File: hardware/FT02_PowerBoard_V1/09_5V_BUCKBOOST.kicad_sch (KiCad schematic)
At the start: 0 parts

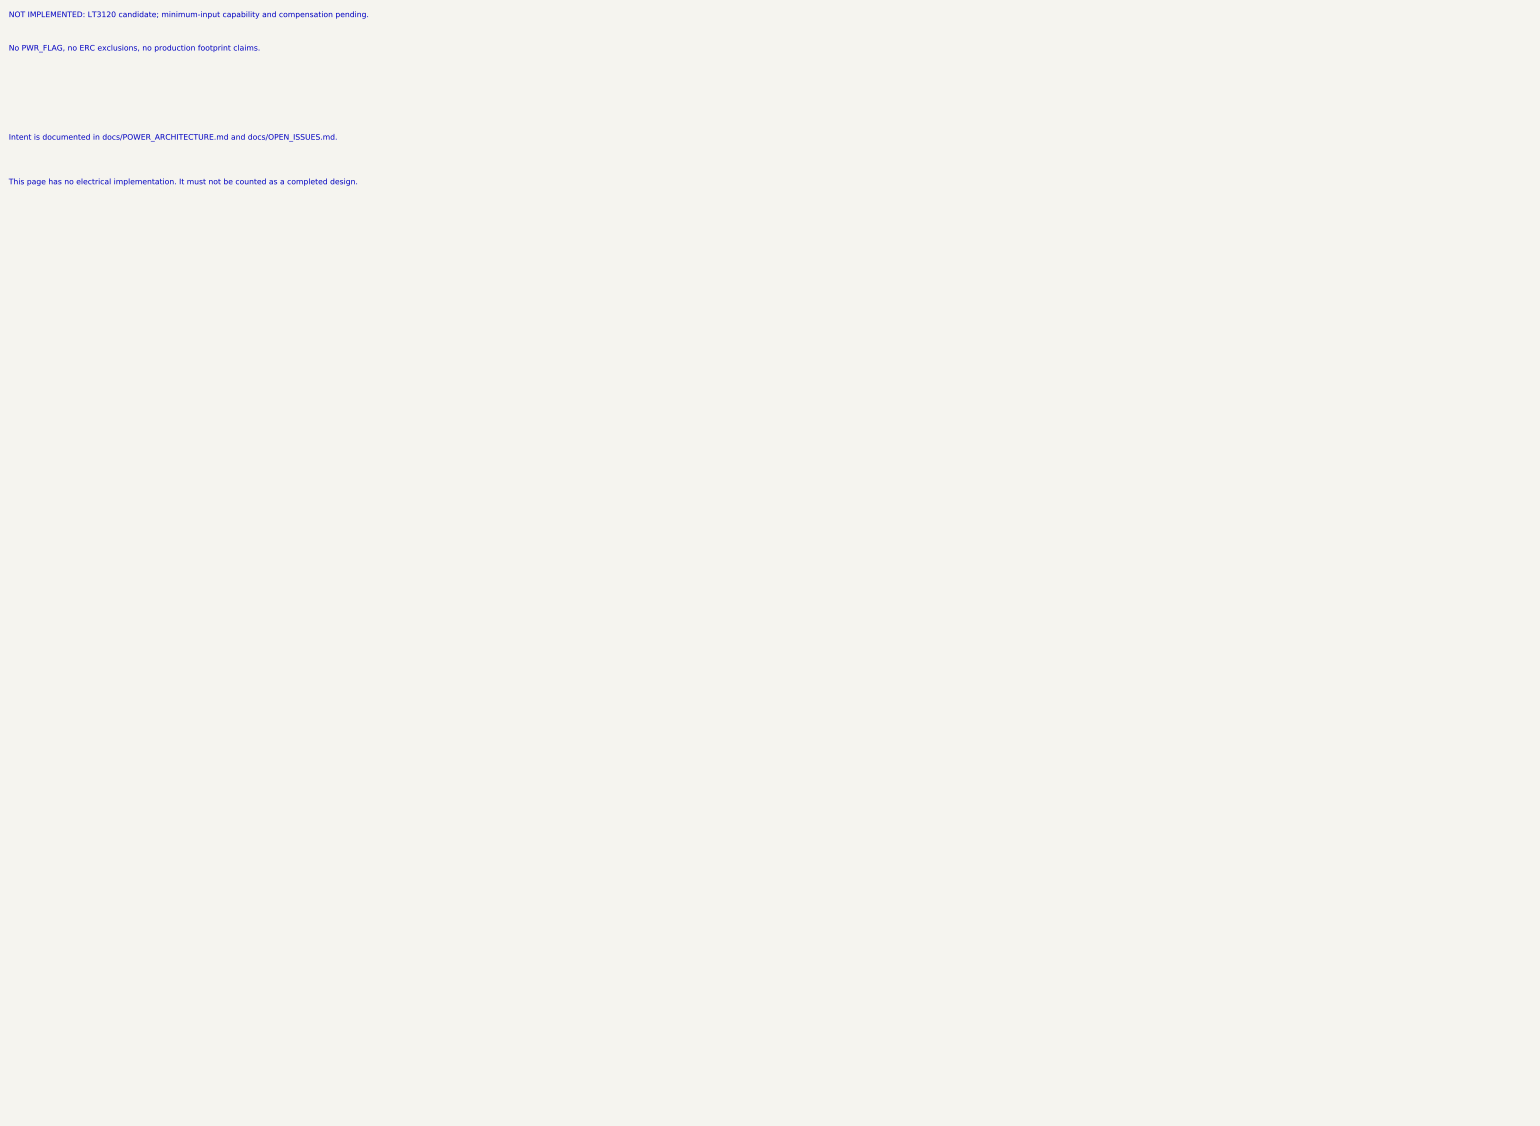
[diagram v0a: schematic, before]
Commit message: Wire FT02 Phase 1 power stages and verify partial shunt boundary
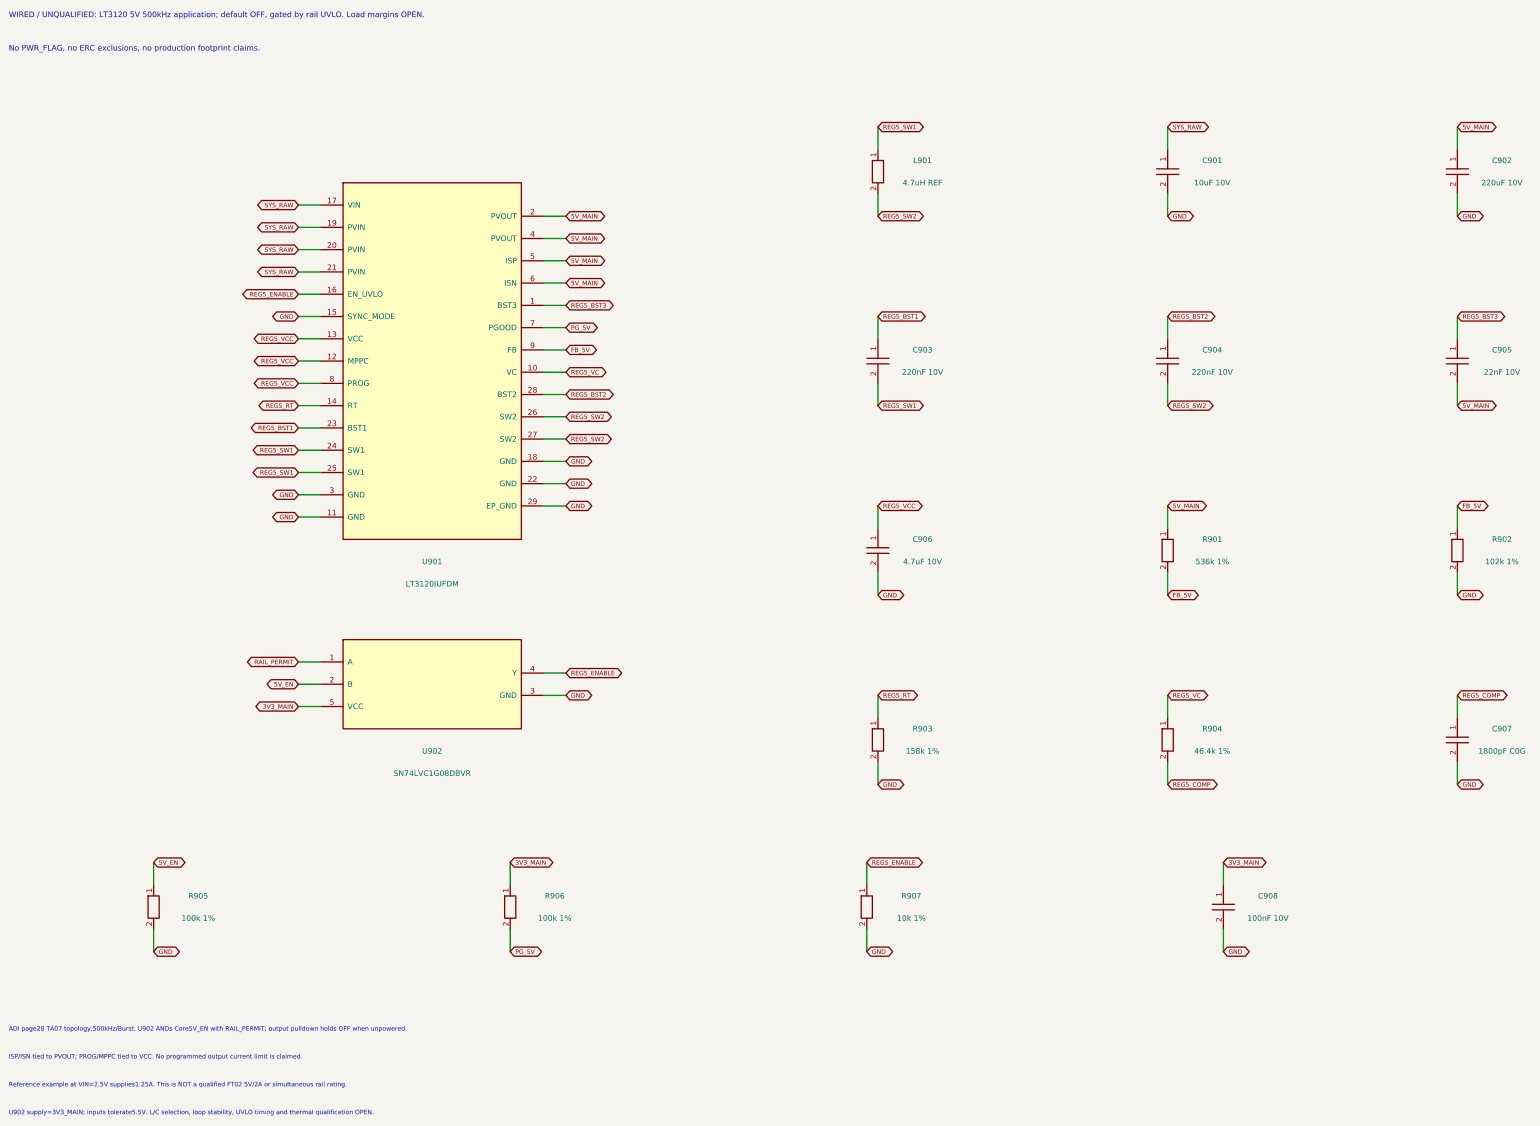
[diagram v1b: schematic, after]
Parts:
- added C901: 10uF 10V, symbol FT02_Reference:C
- added C902: 220uF 10V, symbol FT02_Reference:C
- added C903, C904: 220nF 10V, symbol FT02_Reference:C
- added C905: 22nF 10V, symbol FT02_Reference:C
- added C906: 4.7uF 10V, symbol FT02_Reference:C
- added C907: 1800pF C0G, symbol FT02_Reference:C
- added C908: 100nF 10V, symbol FT02_Reference:C
- added L901: 4.7uH REF, symbol FT02_Reference:L
- added R901: 536k 1%, symbol FT02_Reference:R
- added R902: 102k 1%, symbol FT02_Reference:R
- added R903: 158k 1%, symbol FT02_Reference:R
- added R904: 46.4k 1%, symbol FT02_Reference:R
- added R905, R906: 100k 1%, symbol FT02_Reference:R
- added R907: 10k 1%, symbol FT02_Reference:R
- added U901: LT3120IUFDM, symbol FT02_Reference:LT3120
- added U902: SN74LVC1G08DBVR, symbol FT02_Reference:SN74LVC1G08DBV
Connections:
- new net 3V3_MAIN: C908.1, R906.1, U902.5 (VCC)
- new net 5V_EN: R905.1, U902.2 (B)
- new net 5V_MAIN: C902.1, C905.2, R901.1, U901.2 (PVOUT), U901.4 (PVOUT), U901.5 (ISP), U901.6 (ISN)
- new net FB_5V: R901.2, R902.1, U901.9 (FB)
- new net GND: C901.2, C902.2, C906.2, C907.2, C908.2, R902.2, R903.2, R905.2, R907.2, U901.11 (GND), U901.15 (SYNC_MODE), U901.18 (GND), U901.22 (GND), U901.29 (EP_GND), U901.3 (GND), U902.3 (GND)
- new net PG_5V: R906.2, U901.7 (PGOOD)
- new net RAIL_PERMIT: U902.1 (A)
- new net REG5_BST1: C903.1, U901.23 (BST1)
- new net REG5_BST2: C904.1, U901.28 (BST2)
- new net REG5_BST3: C905.1, U901.1 (BST3)
- new net REG5_COMP: C907.1, R904.2
- new net REG5_ENABLE: R907.1, U901.16 (EN_UVLO), U902.4 (Y)
- new net REG5_RT: R903.1, U901.14 (RT)
- new net REG5_SW1: C903.2, L901.1, U901.24 (SW1), U901.25 (SW1)
- new net REG5_SW2: C904.2, L901.2, U901.26 (SW2), U901.27 (SW2)
- new net REG5_VC: R904.1, U901.10 (VC)
- new net REG5_VCC: C906.1, U901.12 (MPPC), U901.13 (VCC), U901.8 (PROG)
- new net SYS_RAW: C901.1, U901.17 (VIN), U901.19 (PVIN), U901.20 (PVIN), U901.21 (PVIN)
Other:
- note added: "ADI page28 TA07 topology,500kHz/Burst. U902 ANDs Core5V_EN with RAIL_PERMIT; output pulldown holds OFF when unpowered."
- note added: "ISP/ISN tied to PVOUT; PROG/MPPC tied to VCC. No programmed output current limit is claimed."
- note added: "Reference example at VIN=2.5V supplies1.25A. This is NOT a qualified FT02 5V/2A or simultaneous rail rating."
- note added: "U902 supply=3V3_MAIN; inputs tolerate5.5V. L/C selection, loop stability, UVLO timing and thermal qualification OPEN."
- note added: "WIRED / UNQUALIFIED: LT3120 5V 500kHz application; default OFF, gated by rail UVLO. Load margins OPEN."
- note removed: "Intent is documented in docs/POWER_ARCHITECTURE.md and docs/OPEN_ISSUES.md."
- note removed: "NOT IMPLEMENTED: LT3120 candidate; minimum-input capability and compensation pending."
- note removed: "This page has no electrical implementation. It must not be counted as a completed design."
